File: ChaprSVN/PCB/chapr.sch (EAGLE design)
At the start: 20 parts, among them M2 RN42 Module

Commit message: Intermediate version with new power-on circuit.  NOT COMPLETE.
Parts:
- removed LED2: (no value), led:LED3MM
- added D1, D2: 1N4148, diode:1N4148DO35-7
- added PB2: BUTTON, ChapR-Custom:PUSHBUTTON
- added PWR-LED: (no value), led:LED3MM
- added R12, R13, R15: 12k, resistor:R-US_0207/10
- added R14: 22k, resistor:R-US_0207/10
- added T1: (no value), transistor:-PNP-TO92
- added T2: (no value), transistor:-NPN-TO92
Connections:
- net 3.3V renamed +3V3
- new net +5V: ARDUINO.VCC, PB1.1, R12.1, VDIP.5.0V(1), VDIP.5.0V(2), VDIP.5.0V(3)
- new net N$23: ARDUINO.RAWV, T1.C
- new net N$25: D2.A, R15.2, T2.C
- new net N$26: R13.1, T2.B
- new net N$27: D1.C, D2.C, PB2.2
- new net N$29: ARDUINO.A5, D1.A, R12.2
- new net N$30: ARDUINO.A4, R13.2
- net +9V: now also R14.2, T1.E; no longer ARDUINO.RAWV
- net GND: now also PB2.1, PWR-LED.C, T2.E; no longer LED2.C
- net N$1: now also R14.1, R15.1, T1.B; no longer ARDUINO.VCC, PB1.1, VDIP.5.0V(1), VDIP.5.0V(2), VDIP.5.0V(3)
- net N$16: now also PWR-LED.A; no longer LED2.A
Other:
- note added: "PowerOFF"
- note added: "SwitchMonitor"
- moved on the sheet: R1, R2, R3, R4, R5, R6, R7

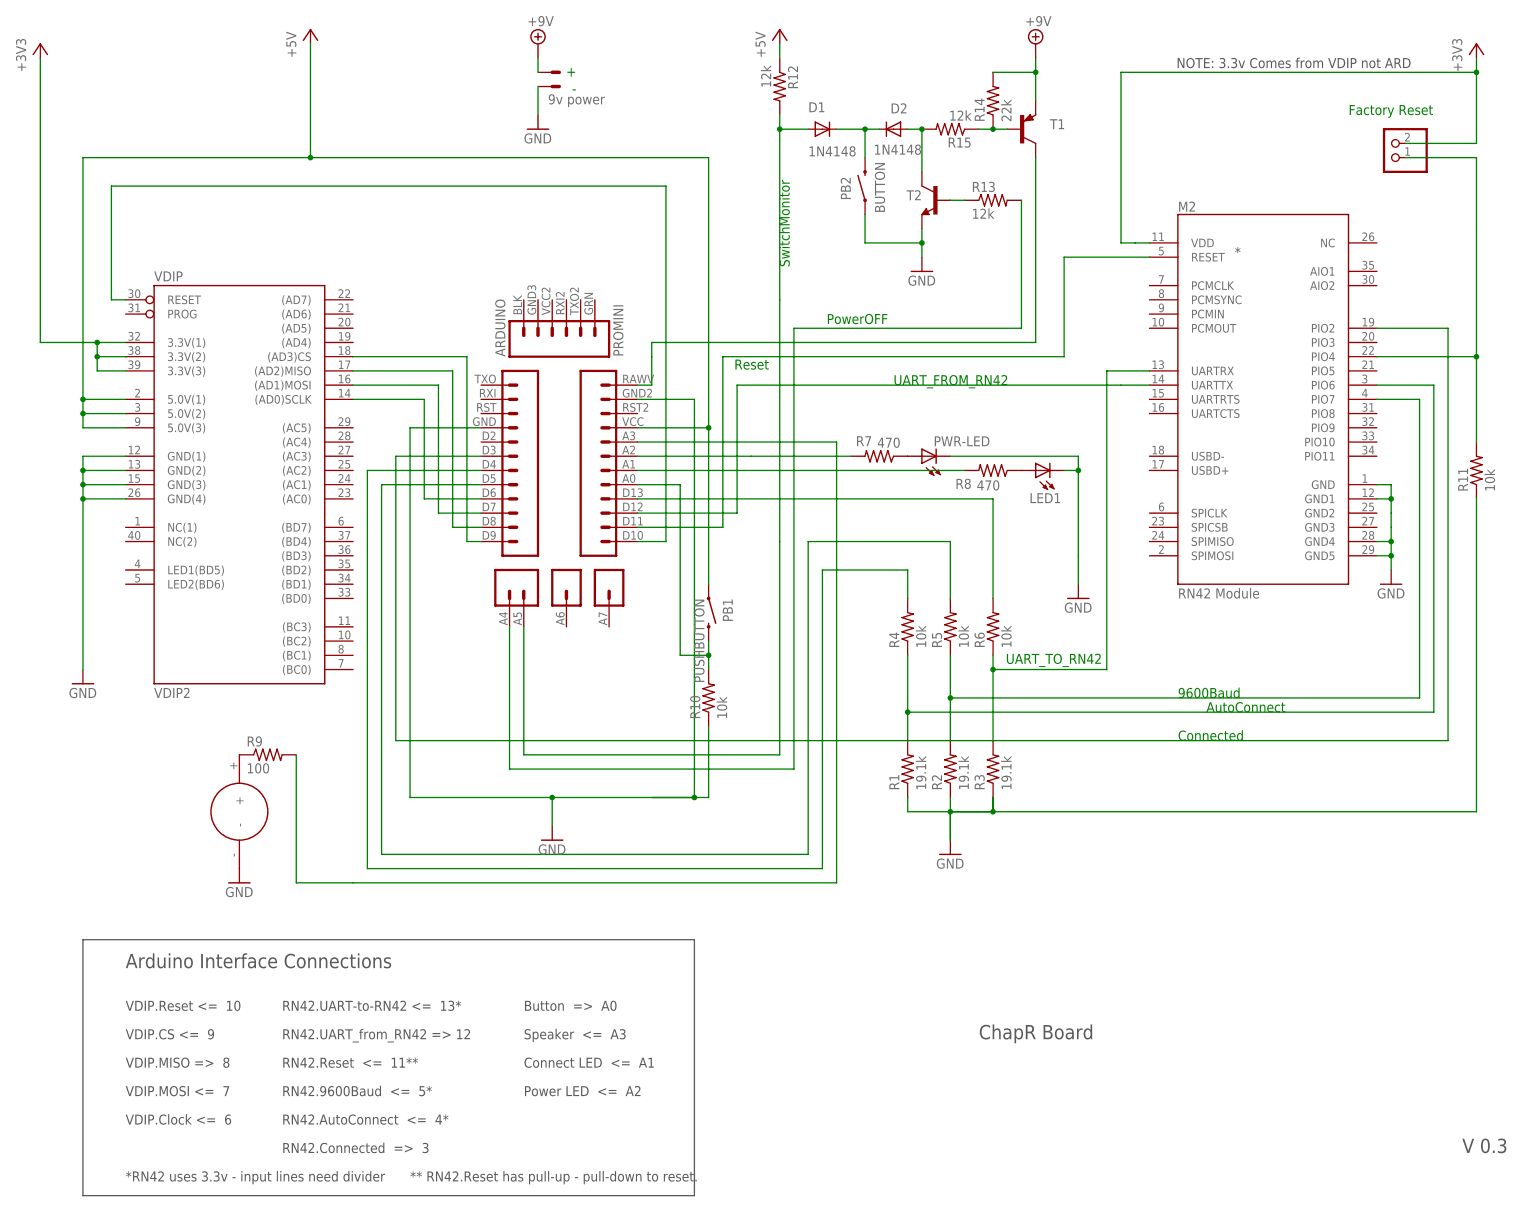
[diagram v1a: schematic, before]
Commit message: 
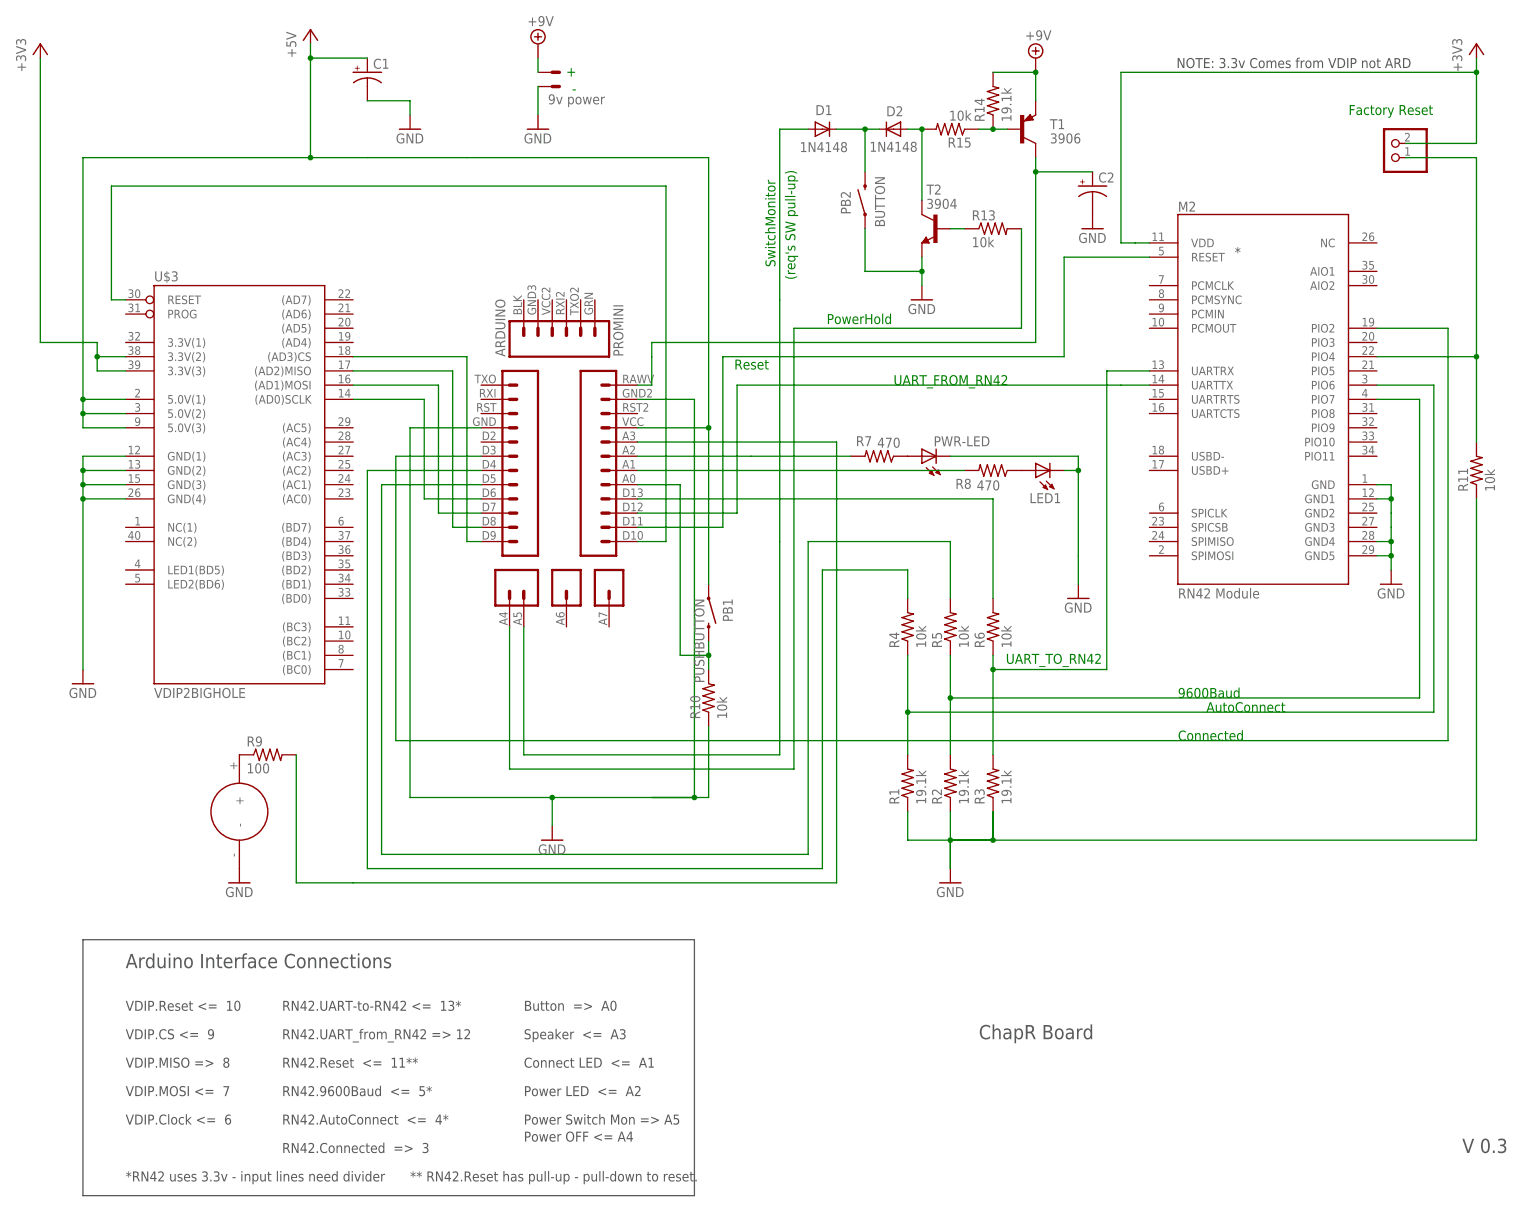
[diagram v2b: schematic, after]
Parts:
- removed R12: 12k, resistor:R-US_0207/10
- removed VDIP: VDIP2, ChapR-Custom:VDIP2
- added C1, C2: (no value), resistor:CPOL-USE2.5-5
- added U$3: VDIP2BIGHOLE, ChapR-Custom:VDIP2BIGHOLE
- R13, R15: value 12k -> 10k
- R14: value 22k -> 19.1k
- T1: value (none) -> 3906
- T2: value (none) -> 3904
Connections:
- net +3V3: now also U$3.3.3V(2), U$3.3.3V(3); no longer VDIP.3.3V(1), VDIP.3.3V(2), VDIP.3.3V(3)
- net +5V: now also C1.+, U$3.5.0V(1), U$3.5.0V(2), U$3.5.0V(3); no longer R12.1, VDIP.5.0V(1), VDIP.5.0V(2), VDIP.5.0V(3)
- net GND: now also C1.-, C2.-, U$3.GND(1), U$3.GND(2), U$3.GND(3), U$3.GND(4); no longer VDIP.GND(1), VDIP.GND(2), VDIP.GND(3), VDIP.GND(4)
- net N$10: now also U$3.(AD3)CS; no longer VDIP.(AD3)CS
- net N$11: now also U$3.(AD2)MISO; no longer VDIP.(AD2)MISO
- net N$12: now also U$3.(AD1)MOSI; no longer VDIP.(AD1)MOSI
- net N$13: now also U$3.(AD0)SCLK; no longer VDIP.(AD0)SCLK
- net N$2: now also U$3.RESET; no longer VDIP.RESET
- net N$23: now also C2.+
- net N$29: no longer R12.2
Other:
- note added: "(req's SW pull-up)"
- note added: "Power OFF <= A4"
- note added: "Power Switch Mon => A5"
- note added: "PowerHold"
- note removed: "PowerOFF"
- moved on the sheet: PB2, R1, R13, R2, R3, T2

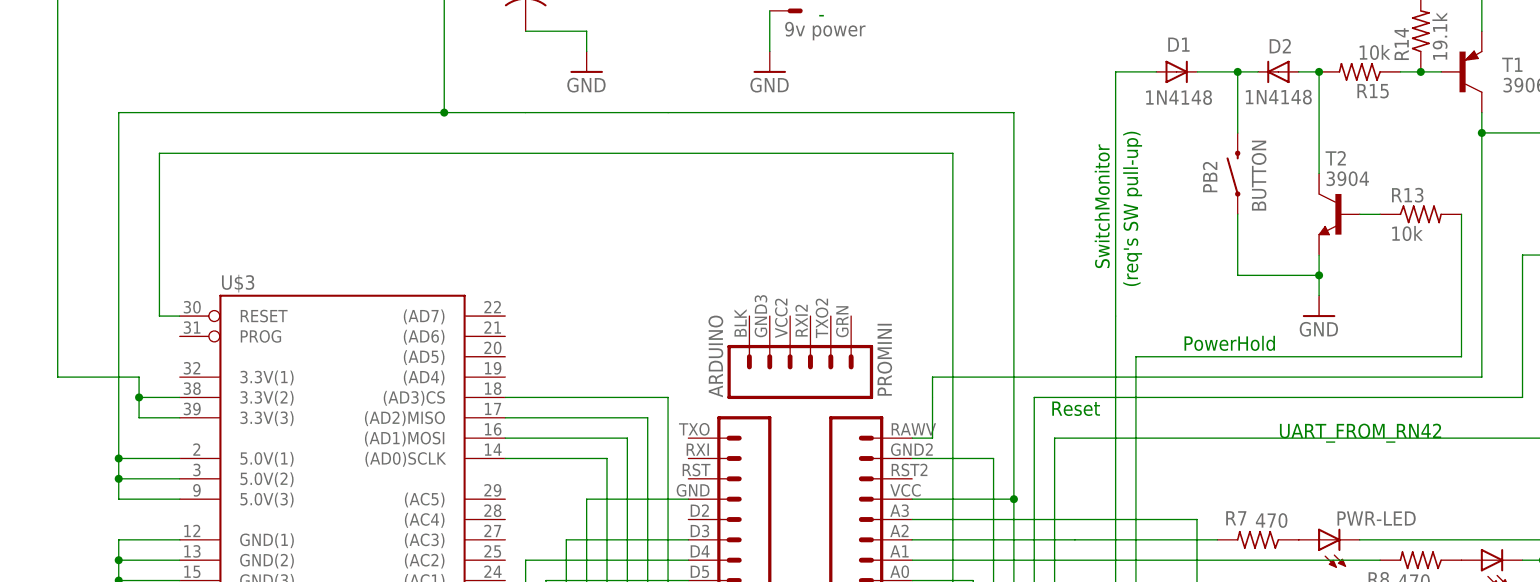
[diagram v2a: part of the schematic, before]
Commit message: 
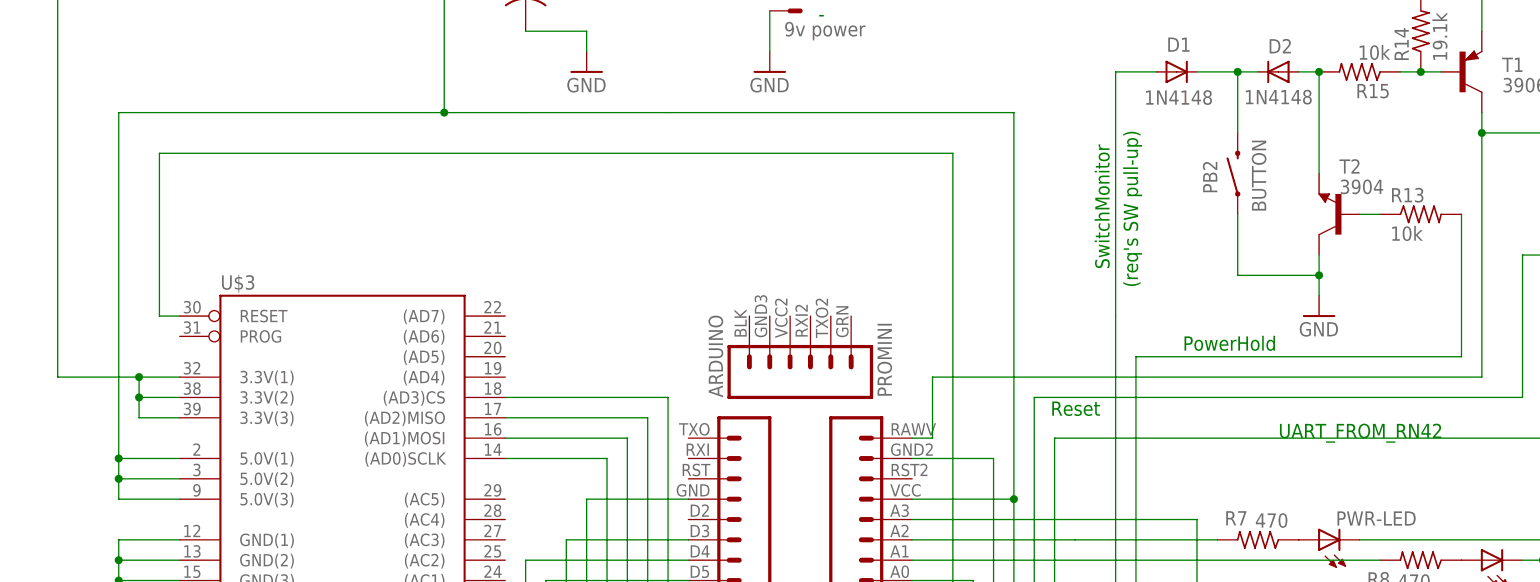
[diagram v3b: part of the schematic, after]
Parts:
- T1: device transistor:-PNP-TO92 -> transistor-neu-to92:-PNP-TO92-EBC
- T2: device transistor:-NPN-TO92 -> transistor-neu-to92:-NPN-TO92-EBC
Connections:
- net +3V3: now also U$3.3.3V(1)
- net GND: now also T2.C; no longer T2.E
- net N$25: now also T2.E; no longer T2.C
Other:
- moved on the sheet: T2
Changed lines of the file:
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@@
 <part name="D2" library="diode" deviceset="1N4148" device="DO35-7" value="1N4148"/>
 <part name="PB2" library="ChapR-Custom" deviceset="PUSHBUTTON" device="" value="BUTTON"/>
-<part name="T1" library="transistor" deviceset="*-PNP-" device="TO92" value="3906"/>
-<part name="T2" library="transistor" deviceset="*-NPN-" device="TO92" value="3904"/>
 <part name="+3V2" library="supply1" deviceset="+3V3" device=""/>
 <part name="SUPPLY1" library="supply2" deviceset="+9V" device=""/>
@@
 <part name="GND9" library="supply1" deviceset="GND" device=""/>
 <part name="GND10" library="supply1" deviceset="GND" device=""/>
+<part name="T1" library="transistor-neu-to92" deviceset="*-PNP-" device="TO92-EBC" value="3906"/>
+<part name="T2" library="transistor-neu-to92" deviceset="*-NPN-" device="TO92-EBC" value="3904"/>
 </parts>
 <sheets>
@@
 <instance part="R11" gate="G$1" x="165.1" y="53.34" rot="R90"/>
 <instance part="R13" gate="G$1" x="78.74" y="96.52"/>
-<instance part="R14" gate="G$1" x="78.74" y="119.38" rot="R90"/>
+<instance part="R14" gate="G$1" x="78.74" y="119.38" smashed="yes" rot="R90">
+<attribute name="NAME" x="77.2414" y="115.57" size="1.778" layer="95" rot="R90"/>
+<attribute name="VALUE" x="82.042" y="115.57" size="1.778" layer="96" rot="R90"/>
+</instance>
 <instance part="R15" gate="G$1" x="71.12" y="114.3" rot="R180"/>
 <instance part="D1" gate="G$1" x="48.26" y="114.3" smashed="yes">
@@
 <attribute name="NAME" x="53.34" y="99.06" size="1.778" layer="95" rot="R90"/>
 <attribute name="VALUE" x="59.436" y="96.774" size="1.778" layer="96" rot="R90"/>
-</instance>
-<instance part="T1" gate="G$1" x="83.82" y="114.3" smashed="yes">
-<attribute name="NAME" x="88.9" y="114.3" size="1.778" layer="95"/>
-<attribute name="VALUE" x="88.9" y="111.76" size="1.778" layer="96"/>
-</instance>
-<instance part="T2" gate="G$1" x="68.58" y="96.52" smashed="yes" rot="MR0">
-<attribute name="NAME" x="69.596" y="102.616" size="1.778" layer="95" rot="MR0"/>
-<attribute name="VALUE" x="72.39" y="100.076" size="1.778" layer="96" rot="MR0"/>
 </instance>
 <instance part="+3V2" gate="G$1" x="165.1" y="129.54"/>
@@
 <instance part="GND9" gate="1" x="-25.4" y="114.3"/>
 <instance part="GND10" gate="1" x="96.52" y="96.52"/>
+<instance part="T1" gate="G$1" x="83.82" y="114.3" smashed="yes">
+<attribute name="NAME" x="88.9" y="114.3" size="1.778" layer="95"/>
+<attribute name="VALUE" x="88.9" y="111.76" size="1.778" layer="96"/>
+</instance>
+<instance part="T2" gate="G$1" x="68.58" y="96.52" smashed="yes" rot="R180">
+<attribute name="NAME" x="68.58" y="101.6" size="1.778" layer="95"/>
+<attribute name="VALUE" x="68.58" y="99.06" size="1.778" layer="96"/>
+</instance>
 </instances>
 <busses>
@@
 </segment>
 <segment>
-<pinref part="T2" gate="G$1" pin="E"/>
 <pinref part="GND8" gate="1" pin="GND"/>
 <wire x1="66.04" y1="91.44" x2="66.04" y2="88.9" width="0.1524" layer="91"/>
@@
 <wire x1="55.88" y1="88.9" x2="66.04" y2="88.9" width="0.1524" layer="91"/>
 <junction x="66.04" y="88.9"/>
+<pinref part="T2" gate="G$1" pin="C"/>
 </segment>
 <segment>
@@
 <segment>
 <pinref part="SUPPLY1" gate="G$1" pin="+9V"/>
-<pinref part="T1" gate="G$1" pin="E"/>
 <pinref part="R14" gate="G$1" pin="2"/>
 <wire x1="86.36" y1="124.46" x2="86.36" y2="119.38" width="0.1524" layer="91"/>
 <wire x1="78.74" y1="124.46" x2="86.36" y2="124.46" width="0.1524" layer="91"/>
 <junction x="86.36" y="124.46"/>
+<pinref part="T1" gate="G$1" pin="E"/>
 </segment>
 </net>
@@
 <pinref part="U$3" gate="G$1" pin="3.3V(2)"/>
 <pinref part="U$3" gate="G$1" pin="3.3V(3)"/>
+<pinref part="U$3" gate="G$1" pin="3.3V(1)"/>
+<wire x1="-76.2" y1="76.2" x2="-81.28" y2="76.2" width="0.1524" layer="91"/>
+<junction x="-81.28" y="76.2"/>
 </segment>
 <segment>
@@
 <segment>
 <pinref part="R14" gate="G$1" pin="1"/>
-<pinref part="T1" gate="G$1" pin="B"/>
 <wire x1="78.74" y1="114.3" x2="81.28" y2="114.3" width="0.1524" layer="91"/>
 <pinref part="R15" gate="G$1" pin="1"/>
 <wire x1="78.74" y1="114.3" x2="76.2" y2="114.3" width="0.1524" layer="91"/>
 <junction x="78.74" y="114.3"/>
+<pinref part="T1" gate="G$1" pin="B"/>
 </segment>
 </net>
@@
 <segment>
 <pinref part="ARDUINO" gate="G$1" pin="RAWV"/>
-<wire x1="17.78" y1="73.66" x2="17.78" y2="68.58" width="0.1524" layer="91"/>
+<wire x1="17.78" y1="76.2" x2="17.78" y2="68.58" width="0.1524" layer="91"/>
 <wire x1="17.78" y1="68.58" x2="15.24" y2="68.58" width="0.1524" layer="91"/>
-<pinref part="T1" gate="G$1" pin="C"/>
 <wire x1="86.36" y1="109.22" x2="86.36" y2="106.68" width="0.1524" layer="91"/>
 <wire x1="86.36" y1="106.68" x2="86.36" y2="76.2" width="0.1524" layer="91"/>
 <wire x1="86.36" y1="76.2" x2="17.78" y2="76.2" width="0.1524" layer="91"/>
-<wire x1="17.78" y1="76.2" x2="17.78" y2="73.66" width="0.1524" layer="91"/>
 <pinref part="C2" gate="G$1" pin="+"/>
 <wire x1="96.52" y1="106.68" x2="86.36" y2="106.68" width="0.1524" layer="91"/>
 <junction x="86.36" y="106.68"/>
+<pinref part="T1" gate="G$1" pin="C"/>
 </segment>
 </net>
@@
 <pinref part="D2" gate="G$1" pin="A"/>
 <wire x1="63.5" y1="114.3" x2="66.04" y2="114.3" width="0.1524" layer="91"/>
-<pinref part="T2" gate="G$1" pin="C"/>
 <wire x1="66.04" y1="114.3" x2="66.04" y2="101.6" width="0.1524" layer="91"/>
 <junction x="66.04" y="114.3"/>
+<pinref part="T2" gate="G$1" pin="E"/>
 </segment>
 </net>
 <net name="N$26" class="0">
 <segment>
-<pinref part="T2" gate="G$1" pin="B"/>
 <pinref part="R13" gate="G$1" pin="1"/>
 <wire x1="73.66" y1="96.52" x2="71.12" y2="96.52" width="0.1524" layer="91"/>
-</segment>
-</net>
+<pinref part="T2" gate="G$1" pin="B"/>
+</segment>
+</net>

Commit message: 
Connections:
- net GND: now also T2.E; no longer T2.C
- net N$25: now also T2.C; no longer T2.E
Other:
- moved on the sheet: T2
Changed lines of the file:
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@@
 <attribute name="VALUE" x="88.9" y="111.76" size="1.778" layer="96"/>
 </instance>
-<instance part="T2" gate="G$1" x="68.58" y="96.52" smashed="yes" rot="R180">
-<attribute name="NAME" x="68.58" y="101.6" size="1.778" layer="95"/>
-<attribute name="VALUE" x="68.58" y="99.06" size="1.778" layer="96"/>
+<instance part="T2" gate="G$1" x="68.58" y="96.52" smashed="yes" rot="MR0">
+<attribute name="NAME" x="68.58" y="91.44" size="1.778" layer="95" rot="MR180"/>
+<attribute name="VALUE" x="68.58" y="93.98" size="1.778" layer="96" rot="MR180"/>
 </instance>
 </instances>
@@
 <segment>
 <pinref part="GND8" gate="1" pin="GND"/>
-<wire x1="66.04" y1="91.44" x2="66.04" y2="88.9" width="0.1524" layer="91"/>
 <pinref part="PB2" gate="G$1" pin="1"/>
 <wire x1="66.04" y1="88.9" x2="66.04" y2="86.36" width="0.1524" layer="91"/>
 <wire x1="55.88" y1="96.52" x2="55.88" y2="88.9" width="0.1524" layer="91"/>
 <wire x1="55.88" y1="88.9" x2="66.04" y2="88.9" width="0.1524" layer="91"/>
+<pinref part="T2" gate="G$1" pin="E"/>
+<wire x1="66.04" y1="88.9" x2="66.04" y2="91.44" width="0.1524" layer="91"/>
 <junction x="66.04" y="88.9"/>
-<pinref part="T2" gate="G$1" pin="C"/>
 </segment>
 <segment>
@@
 <pinref part="D2" gate="G$1" pin="A"/>
 <wire x1="63.5" y1="114.3" x2="66.04" y2="114.3" width="0.1524" layer="91"/>
-<wire x1="66.04" y1="114.3" x2="66.04" y2="101.6" width="0.1524" layer="91"/>
+<pinref part="T2" gate="G$1" pin="C"/>
+<wire x1="66.04" y1="101.6" x2="66.04" y2="114.3" width="0.1524" layer="91"/>
 <junction x="66.04" y="114.3"/>
-<pinref part="T2" gate="G$1" pin="E"/>
-</segment>
-</net>
-<net name="N$26" class="0">
-<segment>
-<pinref part="R13" gate="G$1" pin="1"/>
-<wire x1="73.66" y1="96.52" x2="71.12" y2="96.52" width="0.1524" layer="91"/>
-<pinref part="T2" gate="G$1" pin="B"/>
 </segment>
 </net>
@@
 </segment>
 </net>
+<net name="N$26" class="0">
+<segment>
+<pinref part="T2" gate="G$1" pin="B"/>
+<pinref part="R13" gate="G$1" pin="1"/>
+<wire x1="71.12" y1="96.52" x2="73.66" y2="96.52" width="0.1524" layer="91"/>
+</segment>
+</net>
